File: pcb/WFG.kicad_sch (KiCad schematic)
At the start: 32 parts, among them J1 Conn_01x02_Pin, J2 Conn_01x04_Socket, U1 LM324

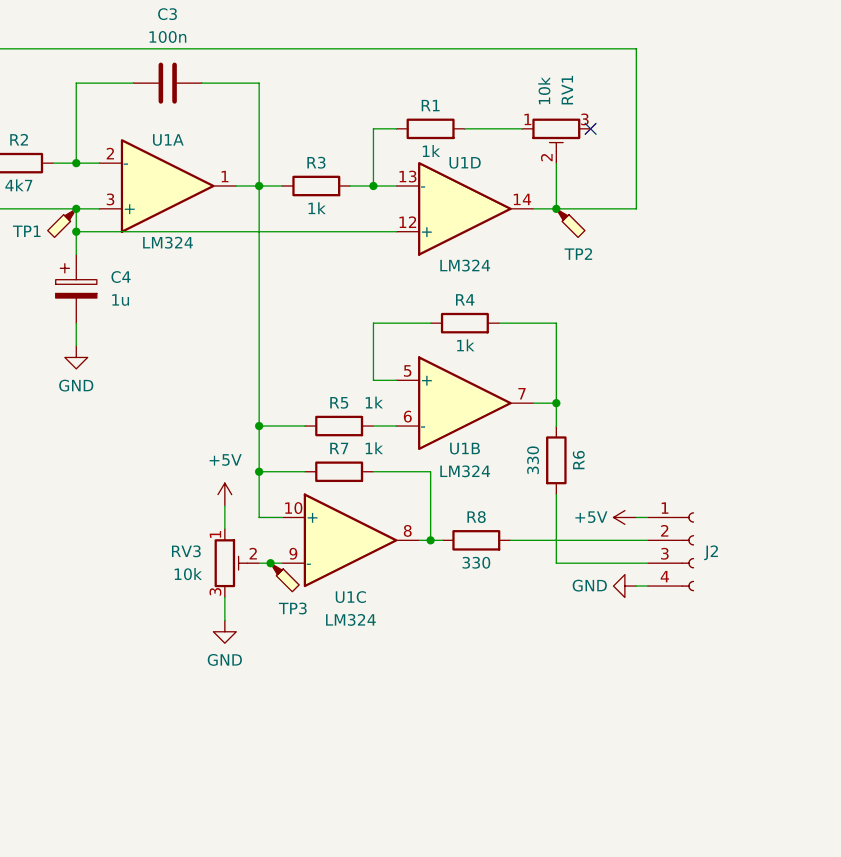
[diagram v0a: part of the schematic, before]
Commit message: Fix LM324 wiring
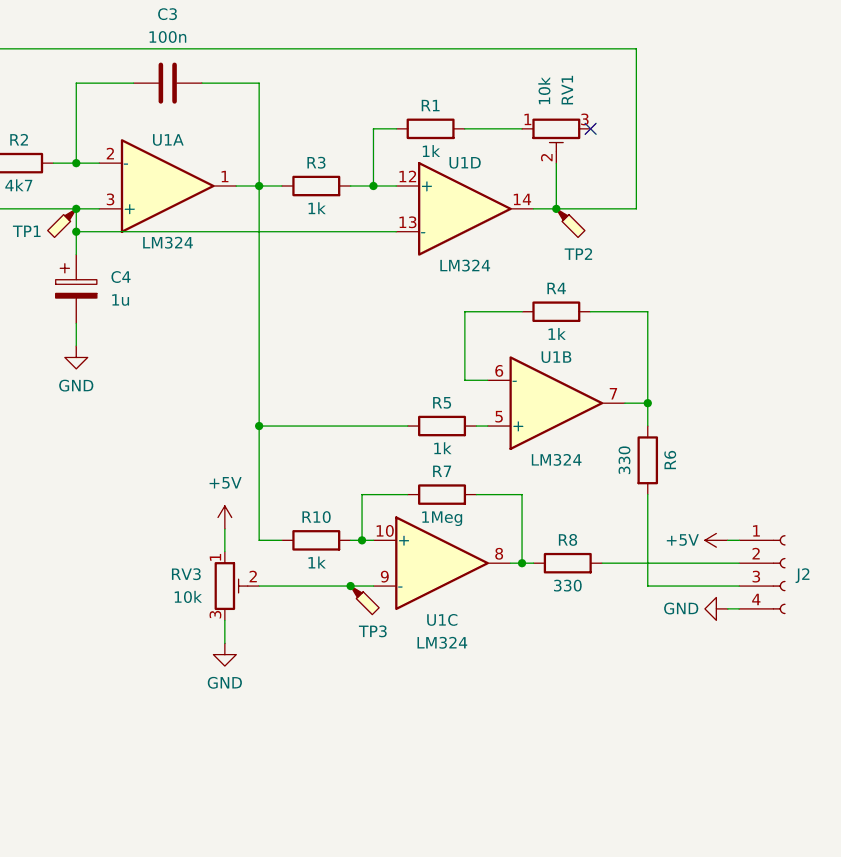
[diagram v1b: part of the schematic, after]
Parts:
- added R10: 1k, Resistor_SMD:R_1206_3216Metric, symbol Device:R
- R7: value 1k -> 1Meg; Nummer 102951 -> 102999
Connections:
- net at C3.2, R3.1, R5.1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: now also R10.1; no longer R7.1, U1.10 (+)
- net at R5.2: now also U1.5 (+); no longer U1.6 (-)
- net at C4.1, RV2.2, TP1.1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: now also U1.13 (-); no longer U1.12 (+)
- net at R1.1, R3.2: now also U1.12 (+); no longer U1.13 (-)
- net at R4.1: now also U1.6 (-); no longer U1.5 (+)
- new net: R10.2, R7.1, U1.10 (+)
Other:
- moved on the sheet: J2, R4, R5, R6, R7, R8, RV3, TP3, U1B, U1C

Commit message: Fix naming of part identifiers
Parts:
- C1: Hersteller HTL -> (none); Nummer 100142 -> (none); Vendor (none) -> HTL; VendorId (none) -> 100142
- C2, C3: Hersteller HTL -> (none); Nummer 100128 -> (none); Vendor (none) -> HTL; VendorId (none) -> 100128
- C4: Hersteller HTL -> (none); Nummer 100139 -> (none); Vendor (none) -> HTL; VendorId (none) -> 100139
- D1: Hersteller HTL -> (none); Nummer 100459 -> (none); Vendor (none) -> HTL; VendorId (none) -> 100459
- F1: Hersteller HTL -> (none); Nummer 101639 -> (none); Vendor (none) -> HTL; VendorId (none) -> 101639
- H1, H2, H3, H4: Hersteller HTL -> (none); Nummer 101018, 101382 -> (none); Vendor (none) -> HTL; VendorId (none) -> 101018, 101382
- J1: Hersteller HTL -> (none); Nummer 101521 -> (none); Vendor (none) -> HTL; VendorId (none) -> 101521
- J2: Nummer 101546 -> (none); VendorId (none) -> 101546
- R1, R10, R3, R4, R5: Hersteller HTL -> (none); Nummer 102951 -> (none); Vendor (none) -> HTL; VendorId (none) -> 102951
- R2: Hersteller HTL -> (none); Nummer 102961 -> (none); Vendor (none) -> HTL; VendorId (none) -> 102961
- R6, R8: Hersteller HTL -> (none); Nummer 102940 -> (none); Vendor (none) -> HTL; VendorId (none) -> 102940
- R7: Hersteller HTL -> (none); Nummer 102999 -> (none); Vendor (none) -> HTL; VendorId (none) -> 102999
- R9: Hersteller HTL -> (none); Nummer 102938 -> (none); Vendor (none) -> HTL; VendorId (none) -> 102938
- RV1, RV2, RV3: Hersteller HTL -> (none); Nummer 100424 -> (none); Vendor (none) -> HTL; VendorId (none) -> 100424
- U1: Hersteller HTL -> (none); Nummer 100324 -> (none); Vendor (none) -> HTL; VendorId (none) -> 100324

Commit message: Add missing vendor
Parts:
- J2: Vendor (none) -> HTL
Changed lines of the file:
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@@
+      (effects (font (size 1.27 1.27)) hide)
+    )
+    (property "Vendor" "HTL" (at 220.98 124.46 0)
       (effects (font (size 1.27 1.27)) hide)
     )
